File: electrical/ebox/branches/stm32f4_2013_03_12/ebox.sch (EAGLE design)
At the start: 0 parts

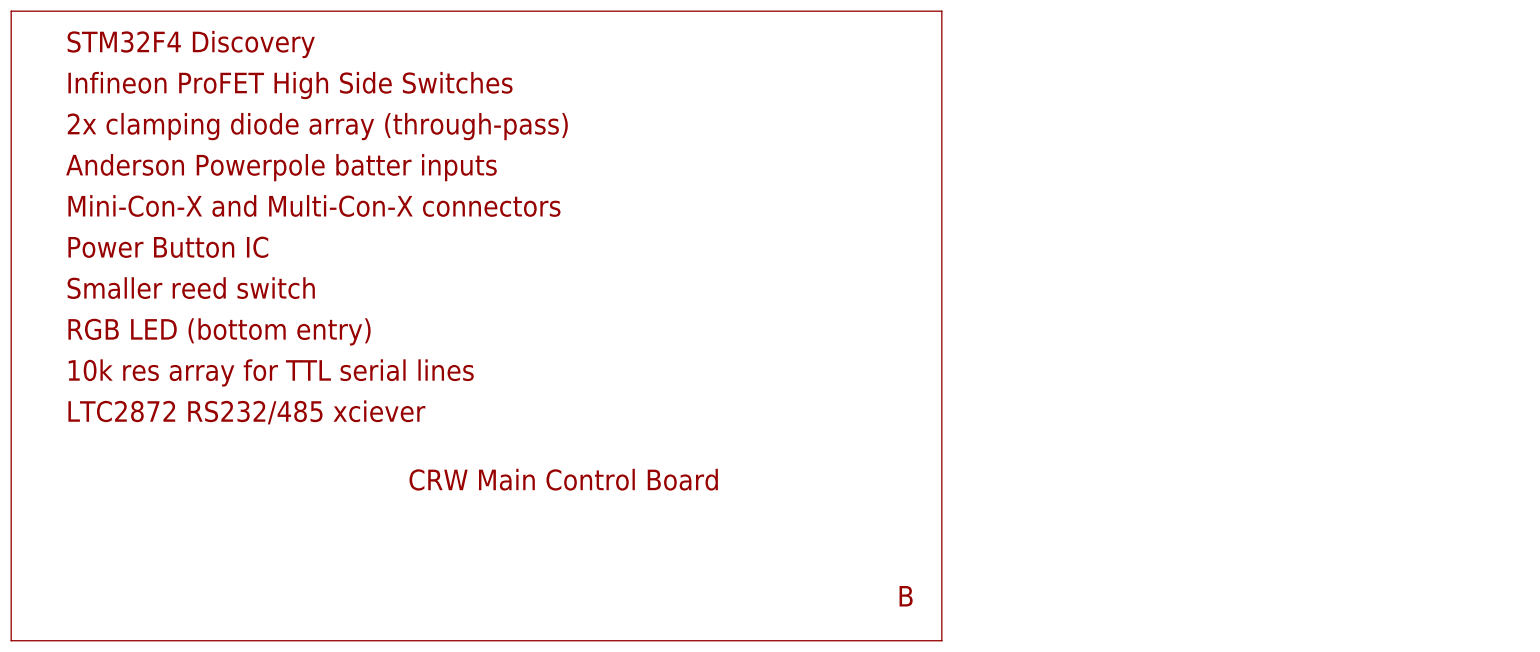
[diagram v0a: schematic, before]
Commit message: Added some docs for new connectors and started making footprints.
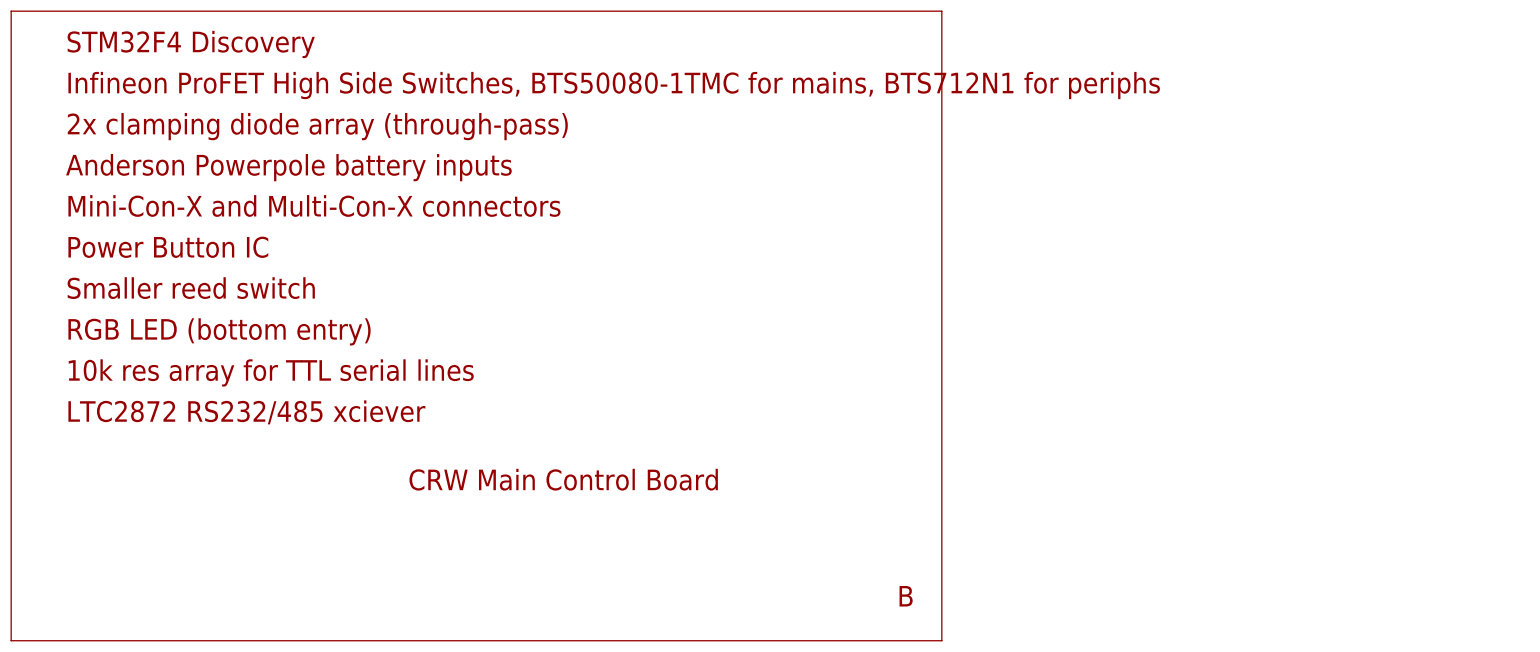
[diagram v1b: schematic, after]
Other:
- note added: "Anderson Powerpole battery inputs"
- note added: "Infineon ProFET High Side Switches, BTS50080‑1TMC for mains, BTS712N1 for periphs"
- note removed: "Anderson Powerpole batter inputs"
- note removed: "Infineon ProFET High Side Switches"
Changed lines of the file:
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@@
 <setting verticaltext="up"/>
 </settings>
-<grid distance="0.1" unitdist="inch" unit="inch" style="lines" multiple="1" display="yes" altdistance="0.01" altunitdist="inch" altunit="inch"/>
+<grid distance="0.1" unitdist="inch" unit="inch" style="lines" multiple="1" display="no" altdistance="0.01" altunitdist="inch" altunit="inch"/>
 <layers>
 <layer number="1" name="Top" color="4" fill="1" visible="no" active="no"/>
@@
 <wire x1="172.72" y1="0" x2="0" y2="0" width="0.1524" layer="94"/>
 <text x="10.16" y="109.22" size="3.81" layer="94" font="vector">STM32F4 Discovery</text>
-<text x="10.16" y="101.6" size="3.81" layer="94" font="vector">Infineon ProFET High Side Switches</text>
+<text x="10.16" y="101.6" size="3.81" layer="94" font="vector">Infineon ProFET High Side Switches, BTS50080‑1TMC for mains, BTS712N1 for periphs</text>
 <text x="10.16" y="93.98" size="3.81" layer="94" font="vector">2x clamping diode array (through-pass)</text>
-<text x="10.16" y="86.36" size="3.81" layer="94" font="vector">Anderson Powerpole batter inputs</text>
+<text x="10.16" y="86.36" size="3.81" layer="94" font="vector">Anderson Powerpole battery inputs</text>
 <text x="10.16" y="78.74" size="3.81" layer="94" font="vector">Mini-Con-X and Multi-Con-X connectors</text>
 <text x="10.16" y="71.12" size="3.81" layer="94" font="vector">Power Button IC</text>
